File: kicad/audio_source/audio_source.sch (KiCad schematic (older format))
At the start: 7 parts, among them J1 SCJ368R1NUS0B00G, P1 CONN_01X01, P2 CONN_01X01, P3 CONN_01X01, P4 CONN_01X01, P5 CONN_01X01, P6 CONN_01X01

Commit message: update
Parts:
- removed P1, P4, P5, P6: CONN_01X01, symbol CONN_01X01
- P1: renamed from P2; value CONN_01X01 -> IN; symbol CONN_01X01 -> CONN_01X03
- P2: renamed from P3; value CONN_01X01 -> OUT; symbol CONN_01X01 -> CONN_01X03
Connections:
- net AGND: now also P1.3 (P3), P2.3 (P3); no longer P1.1 (P1)
- net CD_left_in: now also P1.1 (P1)
- net CD_right_in: now also J1.2, P1.2 (P2); no longer J1.3
- net RADIO_left_out: now also P2.2 (P2)
- net RADIO_right_out: now also J1.3; no longer J1.2
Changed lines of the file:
@@
 $EndDescr
-Wire Wire Line
-	6250 1950 5500 1950
 Wire Wire Line
 	6200 2350 6150 2350
@@
 	6250 1850 6150 1850
 Wire Wire Line
-	6150 2550 6200 2550
-Wire Wire Line
-	6150 2050 6250 2050
-Wire Wire Line
-	5500 1950 5500 2100
+	5400 2550 6200 2550
 $Comp
-L AGND #PWR2
+L AGND #PWR01
 U 1 1 52E56AD2
 P 5250 2500
-F 0 "#PWR2" H 5250 2500 40  0001 C CNN
+F 0 "#PWR01" H 5250 2500 40  0001 C CNN
 F 1 "AGND" H 5250 2430 50  0000 C CNN
 F 2 "" H 5250 2500 60  0001 C CNN
@@
 $EndComp
 $Comp
-L AGND #PWR3
+L AGND #PWR02
 U 1 1 52E56ACB
 P 5500 2100
-F 0 "#PWR3" H 5500 2100 40  0001 C CNN
+F 0 "#PWR02" H 5500 2100 40  0001 C CNN
 F 1 "AGND" H 5500 2030 50  0000 C CNN
 F 2 "" H 5500 2100 60  0001 C CNN
@@
 Text GLabel 6150 1850 0    60   Input ~ 0
 CD_left_in
-Text GLabel 6150 2050 0    60   Input ~ 0
+Text GLabel 6150 1950 0    60   Input ~ 0
 CD_right_in
+Text GLabel 6150 2450 0    60   Input ~ 0
+RADIO_left_out
 Text GLabel 6150 2350 0    60   Input ~ 0
-RADIO_left_out
-Text GLabel 6150 2550 0    60   Input ~ 0
 RADIO_right_out
 $Comp
@@
 	-1   0    0    1
 $EndComp
-Wire Wire Line
-	5250 2450 6200 2450
-Wire Wire Line
-	5250 2450 5250 2500
 Text GLabel 4350 2450 2    60   Input ~ 0
 RADIO_left_out
-Text GLabel 4350 2750 2    60   Input ~ 0
+Text GLabel 4350 2650 2    60   Input ~ 0
 RADIO_right_out
 Text GLabel 4350 2550 2    60   Input ~ 0
 CD_left_in
-Text GLabel 4350 2650 2    60   Input ~ 0
+Text GLabel 4350 2750 2    60   Input ~ 0
 CD_right_in
 $Comp
-L AGND #PWR1
+L AGND #PWR03
 U 1 1 5491D8E0
 P 4150 2950
-F 0 "#PWR1" H 4150 2950 40  0001 C CNN
+F 0 "#PWR03" H 4150 2950 40  0001 C CNN
 F 1 "AGND" H 4150 2880 50  0000 C CNN
 F 2 "" H 4150 2950 60  0001 C CNN
@@
 	4150 2450 4350 2450
 $Comp
-L CONN_01X01 P5
-U 1 1 5491A1C9
-P 6450 1950
-F 0 "P5" H 6450 2050 50  0000 C CNN
-F 1 "CONN_01X01" V 6550 1950 50  0000 C CNN
-F 2 "" H 6450 1950 60  0000 C CNN
-F 3 "" H 6450 1950 60  0000 C CNN
-	1    6450 1950
-	1    0    0    -1
-$EndComp
-$Comp
-L CONN_01X01 P4
-U 1 1 5491A204
-P 6450 1850
-F 0 "P4" H 6450 1950 50  0000 C CNN
-F 1 "CONN_01X01" V 6550 1850 50  0000 C CNN
-F 2 "" H 6450 1850 60  0000 C CNN
-F 3 "" H 6450 1850 60  0000 C CNN
-	1    6450 1850
-	1    0    0    -1
-$EndComp
-$Comp
-L CONN_01X01 P6
-U 1 1 5491A285
-P 6450 2050
-F 0 "P6" H 6450 2150 50  0000 C CNN
-F 1 "CONN_01X01" V 6550 2050 50  0000 C CNN
-F 2 "" H 6450 2050 60  0000 C CNN
-F 3 "" H 6450 2050 60  0000 C CNN
-	1    6450 2050
-	1    0    0    -1
-$EndComp
-$Comp
-L CONN_01X01 P1
-U 1 1 5491A2A2
-P 6400 2350
-F 0 "P1" H 6400 2450 50  0000 C CNN
-F 1 "CONN_01X01" V 6500 2350 50  0000 C CNN
-F 2 "" H 6400 2350 60  0000 C CNN
-F 3 "" H 6400 2350 60  0000 C CNN
-	1    6400 2350
-	1    0    0    -1
-$EndComp
-$Comp
-L CONN_01X01 P2
-U 1 1 5491A2C9
+L CONN_01X03 P2
+U 1 1 5491A2E7
 P 6400 2450
 F 0 "P2" H 6400 2550 50  0000 C CNN
-F 1 "CONN_01X01" V 6500 2450 50  0000 C CNN
+F 1 "OUT" V 6500 2450 50  0000 C CNN
 F 2 "" H 6400 2450 60  0000 C CNN
 F 3 "" H 6400 2450 60  0000 C CNN
@@
 $EndComp
 $Comp
-L CONN_01X01 P3
-U 1 1 5491A2E7
-P 6400 2550
-F 0 "P3" H 6400 2650 50  0000 C CNN
-F 1 "CONN_01X01" V 6500 2550 50  0000 C CNN
-F 2 "" H 6400 2550 60  0000 C CNN
-F 3 "" H 6400 2550 60  0000 C CNN
-	1    6400 2550
+L CONN_01X03 P1
+U 1 1 5491A2C9
+P 6450 1950
+F 0 "P1" H 6450 2050 50  0000 C CNN
+F 1 "IN" V 6550 1950 50  0000 C CNN
+F 2 "" H 6450 1950 60  0000 C CNN
+F 3 "" H 6450 1950 60  0000 C CNN
+	1    6450 1950
 	1    0    0    -1
 $EndComp
+Wire Wire Line
+	5400 2550 5400 2450
+Wire Wire Line
+	5400 2450 5250 2450
+Wire Wire Line
+	5250 2450 5250 2500
+Wire Wire Line
+	6200 2450 6150 2450
+Wire Wire Line
+	5500 2050 6250 2050
+Wire Wire Line
+	5500 2050 5500 2100
+Wire Wire Line
+	6250 1950 6150 1950
 $EndSCHEMATC

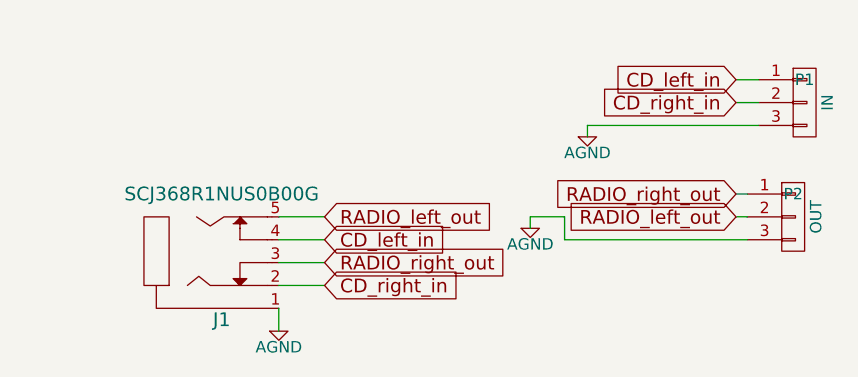
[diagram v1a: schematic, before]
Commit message: jack update to scj-0354-5PU module
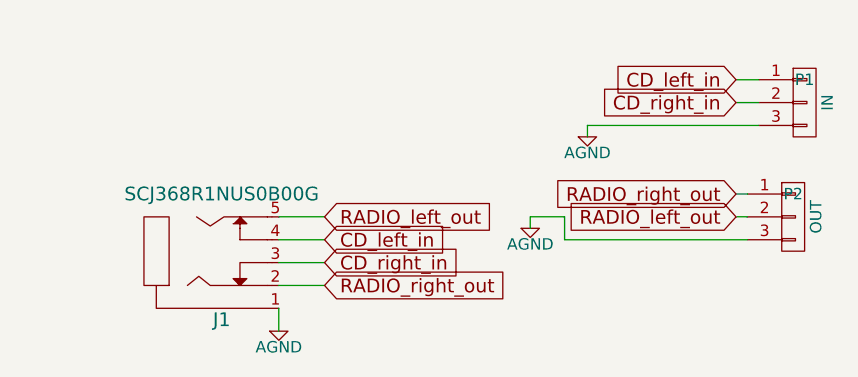
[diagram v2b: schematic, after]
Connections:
- net CD_right_in: now also J1.3; no longer J1.2
- net RADIO_right_out: now also J1.2; no longer J1.3
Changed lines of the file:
@@
 Text GLabel 4350 2450 2    60   Input ~ 0
 RADIO_left_out
-Text GLabel 4350 2650 2    60   Input ~ 0
+Text GLabel 4350 2750 2    60   Input ~ 0
 RADIO_right_out
 Text GLabel 4350 2550 2    60   Input ~ 0
 CD_left_in
-Text GLabel 4350 2750 2    60   Input ~ 0
+Text GLabel 4350 2650 2    60   Input ~ 0
 CD_right_in
 $Comp

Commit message: updates
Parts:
- J1: value SCJ368R1NUS0B00G -> 3.5mmjack; footprint (none) -> jacks:3.5mm_stereo_jack_PJ306M
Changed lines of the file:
@@
 LIBS:memory
 LIBS:xilinx
-LIBS:special
 LIBS:microcontrollers
 LIBS:dsp
@@
 P 3900 2600
 F 0 "J1" H 3900 2900 60  0000 C CNN
-F 1 "SCJ368R1NUS0B00G" H 3900 2350 60  0000 C CNN
-F 2 "" H 3900 2600 60  0000 C CNN
+F 1 "3.5mmjack" H 3900 2350 60  0000 C CNN
+F 2 "jacks:3.5mm_stereo_jack_PJ306M" H 3900 2600 60  0000 C CNN
 F 3 "" H 3900 2600 60  0000 C CNN
 	1    3900 2600
